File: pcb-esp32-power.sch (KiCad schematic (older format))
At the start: 8 parts, among them J1 C-OBD-II-16M, J2 Conn_01x02, J3 Bus_Connector, U1 STEPDOWN12_5

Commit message: Mit SY8008
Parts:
- R1: renamed from R6; value R -> 200k
- R2: renamed from R5; value R -> 390k
- R3: renamed from R16; value 100k -> 470k
- R4: renamed from R17; value 100k -> 470k
- renumbered J3 to J2, J2 to J3
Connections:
- wire segments 36 -> 30
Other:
- moved on the sheet: J3
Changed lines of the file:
@@
 $Descr A4 11693 8268
 encoding utf-8
-Sheet 1 4
+Sheet 1 3
 Title ""
 Date ""
@@
 $EndDescr
 $Comp
-L power:+12V #PWR0108
+L power:+12V #PWR04
 U 1 1 60DA8AE4
 P 3350 1400
-F 0 "#PWR0108" H 3350 1250 50  0001 C CNN
+F 0 "#PWR04" H 3350 1250 50  0001 C CNN
 F 1 "+12V" H 3365 1573 50  0000 C CNN
 F 2 "" H 3350 1400 50  0001 C CNN
@@
 $EndComp
 $Comp
-L power:GND #PWR0109
+L power:GND #PWR05
 U 1 1 60DA924D
 P 3350 1700
-F 0 "#PWR0109" H 3350 1450 50  0001 C CNN
+F 0 "#PWR05" H 3350 1450 50  0001 C CNN
 F 1 "GND" H 3355 1527 50  0000 C CNN
 F 2 "" H 3350 1700 50  0001 C CNN
@@
 $EndComp
 Wire Wire Line
-	3350 1400 3350 1500
-Wire Wire Line
-	3350 1500 3500 1500
-Wire Wire Line
 	3350 1700 3350 1600
 Wire Wire Line
@@
 Wire Wire Line
 	3500 1400 3350 1400
-Connection ~ 3350 1400
-Wire Wire Line
-	3500 1700 3350 1700
-Connection ~ 3350 1700
 Text GLabel 4400 1400 2    50   Input ~ 0
 5VIN
 $Comp
-L power:GND #PWR0110
+L power:GND #PWR07
 U 1 1 60DB30D1
 P 4400 1700
-F 0 "#PWR0110" H 4400 1450 50  0001 C CNN
+F 0 "#PWR07" H 4400 1450 50  0001 C CNN
 F 1 "GND" H 4405 1527 50  0000 C CNN
 F 2 "" H 4400 1700 50  0001 C CNN
@@
 $EndComp
 Wire Wire Line
-	4250 1500 4400 1500
-Wire Wire Line
-	4400 1500 4400 1400
-Wire Wire Line
 	4250 1400 4400 1400
 Wire Wire Line
@@
 Wire Wire Line
 	4400 1600 4400 1700
-Wire Wire Line
-	4250 1700 4400 1700
-Connection ~ 4400 1700
-$Comp
-L power:PWR_FLAG #FLG0101
+$Comp
+L power:PWR_FLAG #FLG02
 U 1 1 60DBE6F2
 P 5750 6900
-F 0 "#FLG0101" H 5750 6975 50  0001 C CNN
+F 0 "#FLG02" H 5750 6975 50  0001 C CNN
 F 1 "PWR_FLAG" H 5750 7073 50  0000 C CNN
 F 2 "" H 5750 6900 50  0001 C CNN
@@
 $EndComp
 $Comp
-L power:+12V #PWR0111
+L power:+12V #PWR010
 U 1 1 60DBEB3A
 P 5750 6900
-F 0 "#PWR0111" H 5750 6750 50  0001 C CNN
+F 0 "#PWR010" H 5750 6750 50  0001 C CNN
 F 1 "+12V" H 5765 7073 50  0000 C CNN
 F 2 "" H 5750 6900 50  0001 C CNN
@@
 $EndComp
 $Comp
-L power:PWR_FLAG #FLG0102
+L power:PWR_FLAG #FLG03
 U 1 1 60DBEFBD
 P 6150 6900
-F 0 "#FLG0102" H 6150 6975 50  0001 C CNN
+F 0 "#FLG03" H 6150 6975 50  0001 C CNN
 F 1 "PWR_FLAG" H 6150 7073 50  0000 C CNN
 F 2 "" H 6150 6900 50  0001 C CNN
@@
 $EndComp
 $Comp
-L power:GND #PWR0112
+L power:GND #PWR011
 U 1 1 60DBF487
 P 6150 6900
-F 0 "#PWR0112" H 6150 6650 50  0001 C CNN
+F 0 "#PWR011" H 6150 6650 50  0001 C CNN
 F 1 "GND" H 6155 6727 50  0000 C CNN
 F 2 "" H 6150 6900 50  0001 C CNN
@@
 $EndComp
 $Comp
-L power:PWR_FLAG #FLG0103
+L power:PWR_FLAG #FLG04
 U 1 1 60D74F1F
 P 6550 6900
-F 0 "#FLG0103" H 6550 6975 50  0001 C CNN
+F 0 "#FLG04" H 6550 6975 50  0001 C CNN
 F 1 "PWR_FLAG" H 6550 7073 50  0000 C CNN
 F 2 "" H 6550 6900 50  0001 C CNN
@@
 $EndComp
 $Comp
-L power:+3.3V #PWR0114
+L power:+3.3V #PWR012
 U 1 1 60D75745
 P 6550 6900
-F 0 "#PWR0114" H 6550 6750 50  0001 C CNN
+F 0 "#PWR012" H 6550 6750 50  0001 C CNN
 F 1 "+3.3V" H 6565 7073 50  0000 C CNN
 F 2 "" H 6550 6900 50  0001 C CNN
@@
 $EndComp
 $Comp
-L Connector_Generic:Conn_01x02 J2
+L Connector_Generic:Conn_01x02 J3
 U 1 1 60EFB4F7
-P 8150 3450
-F 0 "J2" H 8230 3442 50  0000 L CNN
-F 1 "Conn_01x02" H 8230 3351 50  0000 L CNN
-F 2 "Connector_JST:JST_XH_B2B-XH-A_1x02_P2.50mm_Vertical" H 8150 3450 50  0001 C CNN
-F 3 "~" H 8150 3450 50  0001 C CNN
-	1    8150 3450
-	1    0    0    -1
-$EndComp
-$Comp
-L power:+BATT #PWR0101
+P 7100 3350
+F 0 "J3" H 7180 3342 50  0000 L CNN
+F 1 "Conn_01x02" H 7180 3251 50  0000 L CNN
+F 2 "Connector_JST:JST_XH_B2B-XH-A_1x02_P2.50mm_Vertical" H 7100 3350 50  0001 C CNN
+F 3 "~" H 7100 3350 50  0001 C CNN
+	1    7100 3350
+	1    0    0    -1
+$EndComp
+$Comp
+L power:+BATT #PWR013
 U 1 1 60F375B2
-P 7850 3450
-F 0 "#PWR0101" H 7850 3300 50  0001 C CNN
-F 1 "+BATT" H 7865 3623 50  0000 C CNN
-F 2 "" H 7850 3450 50  0001 C CNN
-F 3 "" H 7850 3450 50  0001 C CNN
-	1    7850 3450
-	1    0    0    -1
-$EndComp
-Wire Wire Line
-	7850 3450 7950 3450
-$Comp
-L power:GND #PWR0102
+P 6800 3350
+F 0 "#PWR013" H 6800 3200 50  0001 C CNN
+F 1 "+BATT" H 6815 3523 50  0000 C CNN
+F 2 "" H 6800 3350 50  0001 C CNN
+F 3 "" H 6800 3350 50  0001 C CNN
+	1    6800 3350
+	1    0    0    -1
+$EndComp
+Wire Wire Line
+	6800 3350 6900 3350
+$Comp
+L power:GND #PWR014
 U 1 1 60F38C71
-P 7850 3550
-F 0 "#PWR0102" H 7850 3300 50  0001 C CNN
-F 1 "GND" H 7855 3377 50  0000 C CNN
-F 2 "" H 7850 3550 50  0001 C CNN
-F 3 "" H 7850 3550 50  0001 C CNN
-	1    7850 3550
-	1    0    0    -1
-$EndComp
-Wire Wire Line
-	7850 3550 7950 3550
+P 6800 3450
+F 0 "#PWR014" H 6800 3200 50  0001 C CNN
+F 1 "GND" H 6805 3277 50  0000 C CNN
+F 2 "" H 6800 3450 50  0001 C CNN
+F 3 "" H 6800 3450 50  0001 C CNN
+	1    6800 3450
+	1    0    0    -1
+$EndComp
+Wire Wire Line
+	6800 3450 6900 3450
 $Comp
 L stepdown12_5:STEPDOWN12_5 U1
@@
 5VIN
 $Comp
-L Device:R R6
+L Device:R R1
 U 1 1 60F6141D
 P 5550 1550
-F 0 "R6" H 5620 1596 50  0000 L CNN
-F 1 "R" H 5620 1505 50  0000 L CNN
+F 0 "R1" H 5620 1596 50  0000 L CNN
+F 1 "200k" H 5620 1505 50  0000 L CNN
 F 2 "Resistor_SMD:R_0603_1608Metric_Pad0.98x0.95mm_HandSolder" V 5480 1550 50  0001 C CNN
 F 3 "~" H 5550 1550 50  0001 C CNN
@@
 $EndComp
 $Comp
-L Device:R R5
+L Device:R R2
 U 1 1 60F61A44
 P 5550 1950
-F 0 "R5" H 5620 1996 50  0000 L CNN
-F 1 "R" H 5620 1905 50  0000 L CNN
+F 0 "R2" H 5620 1996 50  0000 L CNN
+F 1 "390k" H 5620 1905 50  0000 L CNN
 F 2 "Resistor_SMD:R_0603_1608Metric_Pad0.98x0.95mm_HandSolder" V 5480 1950 50  0001 C CNN
 F 3 "~" H 5550 1950 50  0001 C CNN
@@
 	5550 1750 5550 1800
 $Comp
-L power:GND #PWR0120
+L power:GND #PWR09
 U 1 1 60F64C82
 P 5550 2100
-F 0 "#PWR0120" H 5550 1850 50  0001 C CNN
+F 0 "#PWR09" H 5550 1850 50  0001 C CNN
 F 1 "GND" H 5555 1927 50  0000 C CNN
 F 2 "" H 5550 2100 50  0001 C CNN
@@
 INT
 $Comp
-L ESP32_Bus:Bus_Connector J3
+L ESP32_Bus:Bus_Connector J2
 U 1 1 60F7276E
 P 3100 3850
-F 0 "J3" H 3100 4593 60  0000 C CNN
+F 0 "J2" H 3100 4593 60  0000 C CNN
 F 1 "Bus_Connector" H 3100 4487 60  0000 C CNN
 F 2 "esp32bus:PinHeader" H 3100 4381 60  0000 C CNN
@@
 	3600 4000 3700 4000
 $Comp
-L power:GND #PWR0121
+L power:GND #PWR06
 U 1 1 60F7A061
 P 3700 3400
-F 0 "#PWR0121" H 3700 3150 50  0001 C CNN
+F 0 "#PWR06" H 3700 3150 50  0001 C CNN
 F 1 "GND" H 3705 3227 50  0000 C CNN
 F 2 "" H 3700 3400 50  0001 C CNN
@@
 	3700 3500 3700 3400
 $Comp
-L power:+3.3V #PWR0122
+L power:+3.3V #PWR03
 U 1 1 60F7BA28
 P 2450 3400
-F 0 "#PWR0122" H 2450 3250 50  0001 C CNN
+F 0 "#PWR03" H 2450 3250 50  0001 C CNN
 F 1 "+3.3V" H 2465 3573 50  0000 C CNN
 F 2 "" H 2450 3400 50  0001 C CNN
@@
 $EndComp
 $Comp
-L power:+12V #PWR0106
+L power:+12V #PWR02
 U 1 1 6103B5E2
 P 2400 1900
-F 0 "#PWR0106" H 2400 1750 50  0001 C CNN
+F 0 "#PWR02" H 2400 1750 50  0001 C CNN
 F 1 "+12V" H 2415 2073 50  0000 C CNN
 F 2 "" H 2400 1900 50  0001 C CNN
@@
 CANL
 $Comp
-L power:GND #PWR0107
+L power:GND #PWR01
 U 1 1 6103C4CA
 P 1100 1600
-F 0 "#PWR0107" H 1100 1350 50  0001 C CNN
+F 0 "#PWR01" H 1100 1350 50  0001 C CNN
 F 1 "GND" H 1105 1427 50  0000 C CNN
 F 2 "" H 1100 1600 50  0001 C CNN
@@
 NoConn ~ 2250 1200
 $Sheet
-S 8750 2200 1200 850
+S 9800 650  1200 850
 U 612652A3
 F0 "TP4054" 50
@@
 $EndSheet
 $Sheet
-S 9100 3550 1100 950
+S 9900 1750 1100 950
 U 612B5E8A
 F0 "SY8008" 50
 F1 "sy8008/sy8008.sch" 50
-$EndSheet
-$Sheet
-S 9100 4900 1150 950
-U 612FA5D2
-F0 "LTC3530" 50
-F1 "ltc3530/ltc3530.sch" 50
 $EndSheet
 Wire Wire Line
@@
 BATTVOLT
 $Comp
-L power:+BATT #PWR0116
+L power:+BATT #PWR015
 U 1 1 6131DA4C
 P 7000 1400
-F 0 "#PWR0116" H 7000 1250 50  0001 C CNN
+F 0 "#PWR015" H 7000 1250 50  0001 C CNN
 F 1 "+BATT" H 7015 1573 50  0000 C CNN
 F 2 "" H 7000 1400 50  0001 C CNN
@@
 $EndComp
 $Comp
-L Device:R R16
+L Device:R R3
 U 1 1 6131E154
 P 7000 1550
-F 0 "R16" H 7070 1596 50  0000 L CNN
-F 1 "100k" H 7070 1505 50  0000 L CNN
+F 0 "R3" H 7070 1596 50  0000 L CNN
+F 1 "470k" H 7070 1505 50  0000 L CNN
 F 2 "Resistor_SMD:R_0603_1608Metric_Pad0.98x0.95mm_HandSolder" V 6930 1550 50  0001 C CNN
 F 3 "~" H 7000 1550 50  0001 C CNN
@@
 $EndComp
 $Comp
-L Device:R R17
+L Device:R R4
 U 1 1 6131E8A9
 P 7000 1950
-F 0 "R17" H 7070 1996 50  0000 L CNN
-F 1 "100k" H 7070 1905 50  0000 L CNN
+F 0 "R4" H 7070 1996 50  0000 L CNN
+F 1 "470k" H 7070 1905 50  0000 L CNN
 F 2 "Resistor_SMD:R_0603_1608Metric_Pad0.98x0.95mm_HandSolder" V 6930 1950 50  0001 C CNN
 F 3 "~" H 7000 1950 50  0001 C CNN
@@
 $EndComp
 $Comp
-L power:GND #PWR0117
+L power:GND #PWR016
 U 1 1 6131ED93
 P 7000 2100
-F 0 "#PWR0117" H 7000 1850 50  0001 C CNN
+F 0 "#PWR016" H 7000 1850 50  0001 C CNN
 F 1 "GND" H 7005 1927 50  0000 C CNN
 F 2 "" H 7000 2100 50  0001 C CNN
@@
 NoConn ~ 4650 3850
 NoConn ~ 4650 4000
+$Comp
+L power:+BATT #PWR08
+U 1 1 61364414
+P 5300 6900
+F 0 "#PWR08" H 5300 6750 50  0001 C CNN
+F 1 "+BATT" H 5315 7073 50  0000 C CNN
+F 2 "" H 5300 6900 50  0001 C CNN
+F 3 "" H 5300 6900 50  0001 C CNN
+	1    5300 6900
+	-1   0    0    1
+$EndComp
+$Comp
+L power:PWR_FLAG #FLG01
+U 1 1 61365091
+P 5300 6900
+F 0 "#FLG01" H 5300 6975 50  0001 C CNN
+F 1 "PWR_FLAG" H 5300 7073 50  0000 C CNN
+F 2 "" H 5300 6900 50  0001 C CNN
+F 3 "~" H 5300 6900 50  0001 C CNN
+	1    5300 6900
+	1    0    0    -1
+$EndComp
 $EndSCHEMATC

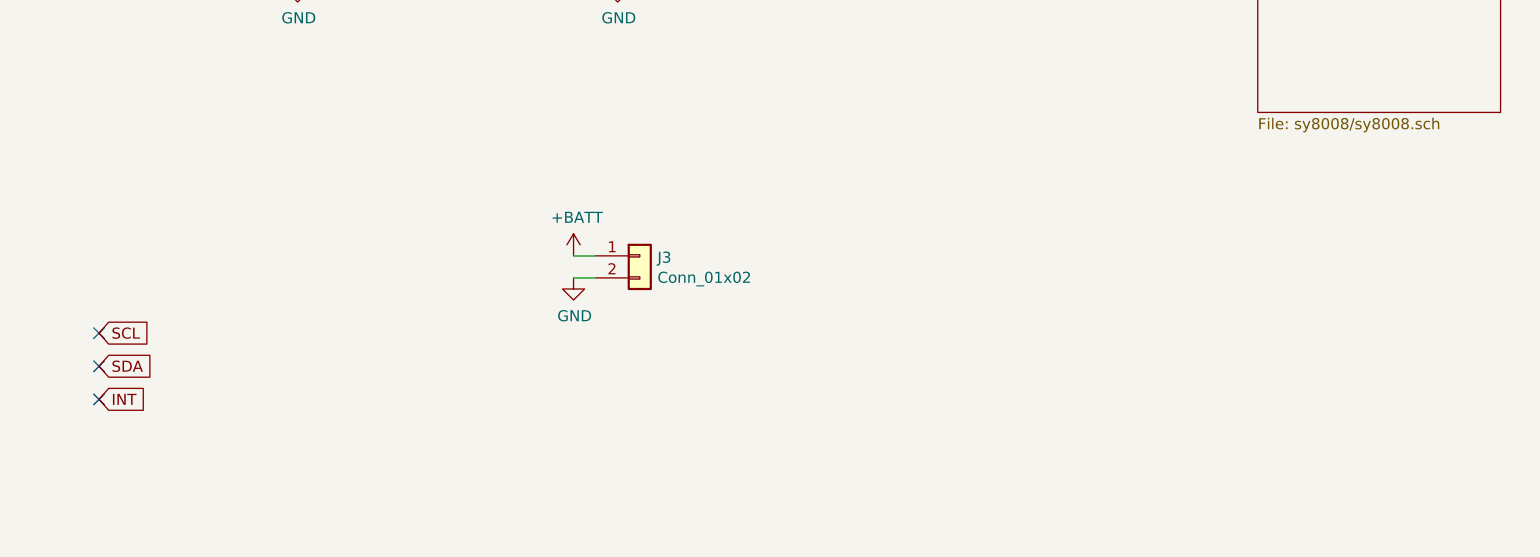
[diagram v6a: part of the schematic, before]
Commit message: Mit Sy8008 und LTC3530
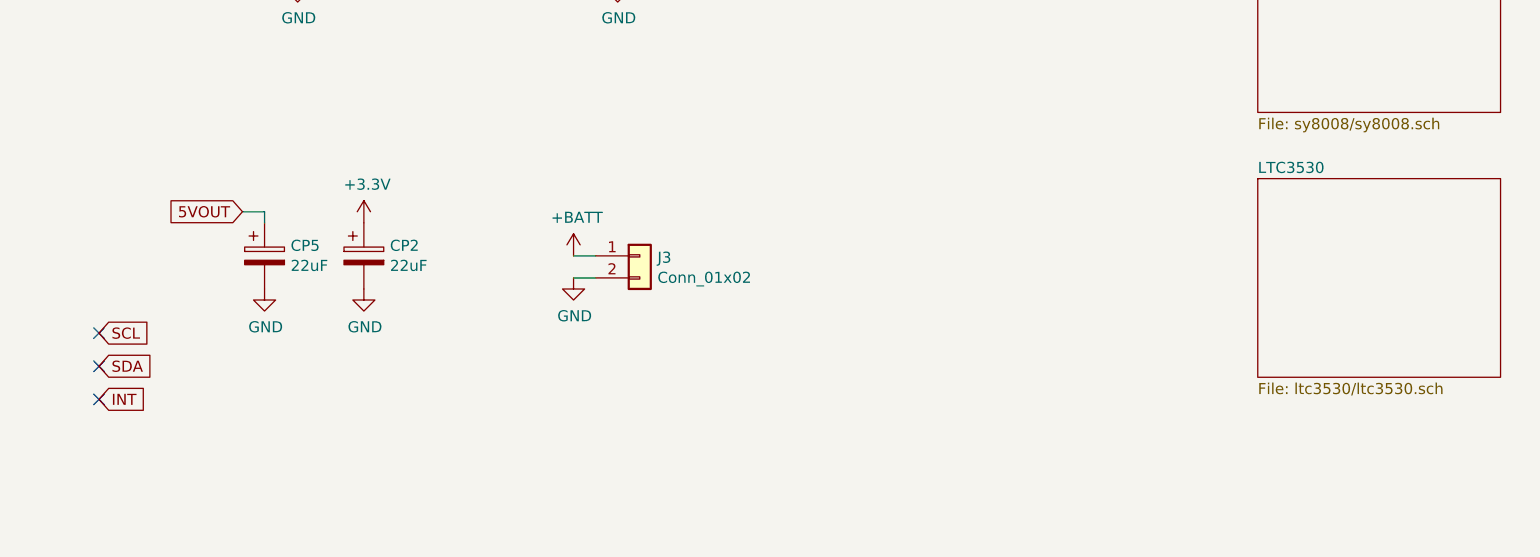
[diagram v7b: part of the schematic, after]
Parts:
- added CP2, CP5: 22uF, Capacitor_Tantalum_SMD:CP_EIA-6032-28_Kemet-C_Pad2.25x2.35mm_HandSolder, symbol Device:CP
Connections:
- net +3V3: now also CP2.1
- net GND: now also CP2.2, CP5.2
- new net 5VOUT: CP5.1
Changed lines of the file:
@@
 $Descr A4 11693 8268
 encoding utf-8
-Sheet 1 3
+Sheet 1 4
 Title ""
 Date ""
@@
 	1    0    0    -1
 $EndComp
+$Sheet
+S 9900 3000 1100 900
+U 613584C2
+F0 "LTC3530" 50
+F1 "ltc3530/ltc3530.sch" 50
+$EndSheet
+$Comp
+L power:+3.3V #PWR0103
+U 1 1 6135B72B
+P 5850 3200
+F 0 "#PWR0103" H 5850 3050 50  0001 C CNN
+F 1 "+3.3V" H 5865 3373 50  0000 C CNN
+F 2 "" H 5850 3200 50  0001 C CNN
+F 3 "" H 5850 3200 50  0001 C CNN
+	1    5850 3200
+	1    0    0    -1
+$EndComp
+$Comp
+L Device:CP CP2
+U 1 1 6135C742
+P 5850 3350
+F 0 "CP2" H 5968 3396 50  0000 L CNN
+F 1 "22uF" H 5968 3305 50  0000 L CNN
+F 2 "Capacitor_Tantalum_SMD:CP_EIA-6032-28_Kemet-C_Pad2.25x2.35mm_HandSolder" H 5888 3200 50  0001 C CNN
+F 3 "~" H 5850 3350 50  0001 C CNN
+	1    5850 3350
+	1    0    0    -1
+$EndComp
+$Comp
+L power:GND #PWR0104
+U 1 1 6135CC65
+P 5850 3500
+F 0 "#PWR0104" H 5850 3250 50  0001 C CNN
+F 1 "GND" H 5855 3327 50  0000 C CNN
+F 2 "" H 5850 3500 50  0001 C CNN
+F 3 "" H 5850 3500 50  0001 C CNN
+	1    5850 3500
+	1    0    0    -1
+$EndComp
+Text GLabel 5300 3150 0    50   Input ~ 0
+5VOUT
+$Comp
+L Device:CP CP5
+U 1 1 6136F84A
+P 5400 3350
+F 0 "CP5" H 5518 3396 50  0000 L CNN
+F 1 "22uF" H 5518 3305 50  0000 L CNN
+F 2 "Capacitor_Tantalum_SMD:CP_EIA-6032-28_Kemet-C_Pad2.25x2.35mm_HandSolder" H 5438 3200 50  0001 C CNN
+F 3 "~" H 5400 3350 50  0001 C CNN
+	1    5400 3350
+	1    0    0    -1
+$EndComp
+$Comp
+L power:GND #PWR0105
+U 1 1 6136FEB6
+P 5400 3500
+F 0 "#PWR0105" H 5400 3250 50  0001 C CNN
+F 1 "GND" H 5405 3327 50  0000 C CNN
+F 2 "" H 5400 3500 50  0001 C CNN
+F 3 "" H 5400 3500 50  0001 C CNN
+	1    5400 3500
+	1    0    0    -1
+$EndComp
+Wire Wire Line
+	5300 3150 5400 3150
+Wire Wire Line
+	5400 3150 5400 3200
 $EndSCHEMATC

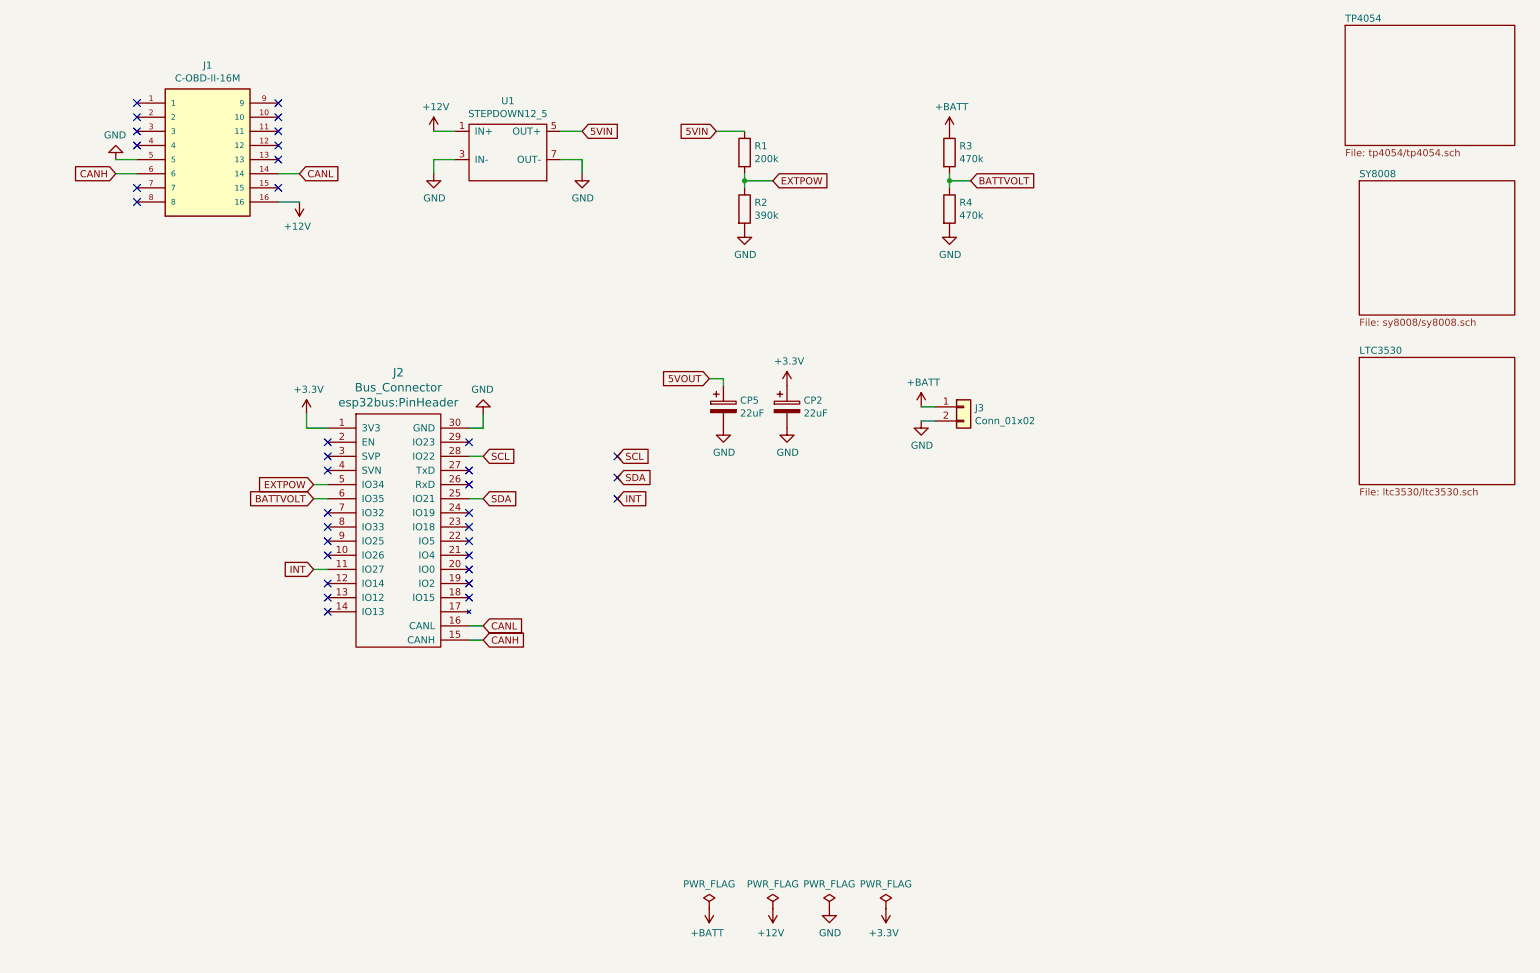
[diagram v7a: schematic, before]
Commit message: LED zugefügt
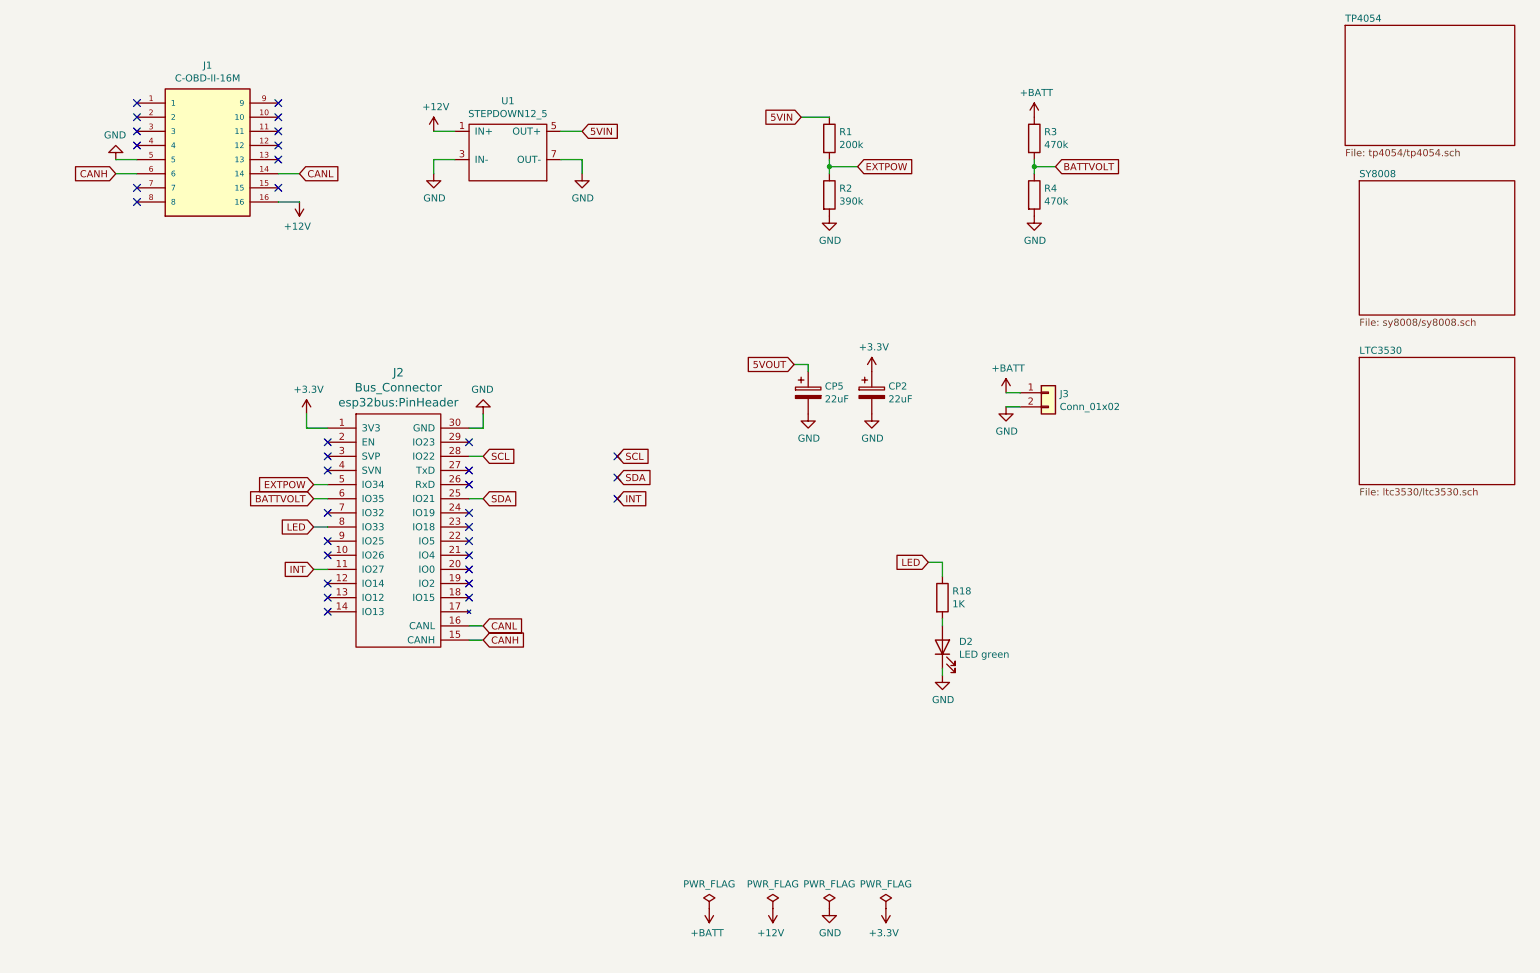
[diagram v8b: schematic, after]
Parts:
- added D2: LED green, LED_SMD:LED_0805_2012Metric_Pad1.15x1.40mm_HandSolder, symbol Device:LED
- added R18: 1K, Resistor_SMD:R_0603_1608Metric_Pad0.98x0.95mm_HandSolder, symbol Device:R
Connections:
- net GND: now also D2.1 (K)
- net LED: now reaches J2.8 (IO33)
- net LED: now also R18.1
- new net: D2.2 (A), R18.2
- no-connect marks 35 -> 34
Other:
- moved on the sheet: CP2, CP5, J3, R1, R2, R3, R4
